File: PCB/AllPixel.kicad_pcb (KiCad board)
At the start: 2 copper layers, 68.5 x 24.5 mm, 28 parts, among them CON1 ML_USB_MINI, CON2 BARREL_JACK, Q1 NPN, U1 ATMEGA16U4/32U4, Y1 16MHz

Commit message: fixed silk screen on pads
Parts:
- U1: footprint TQFP44 -> TQFP44_FixedSilk

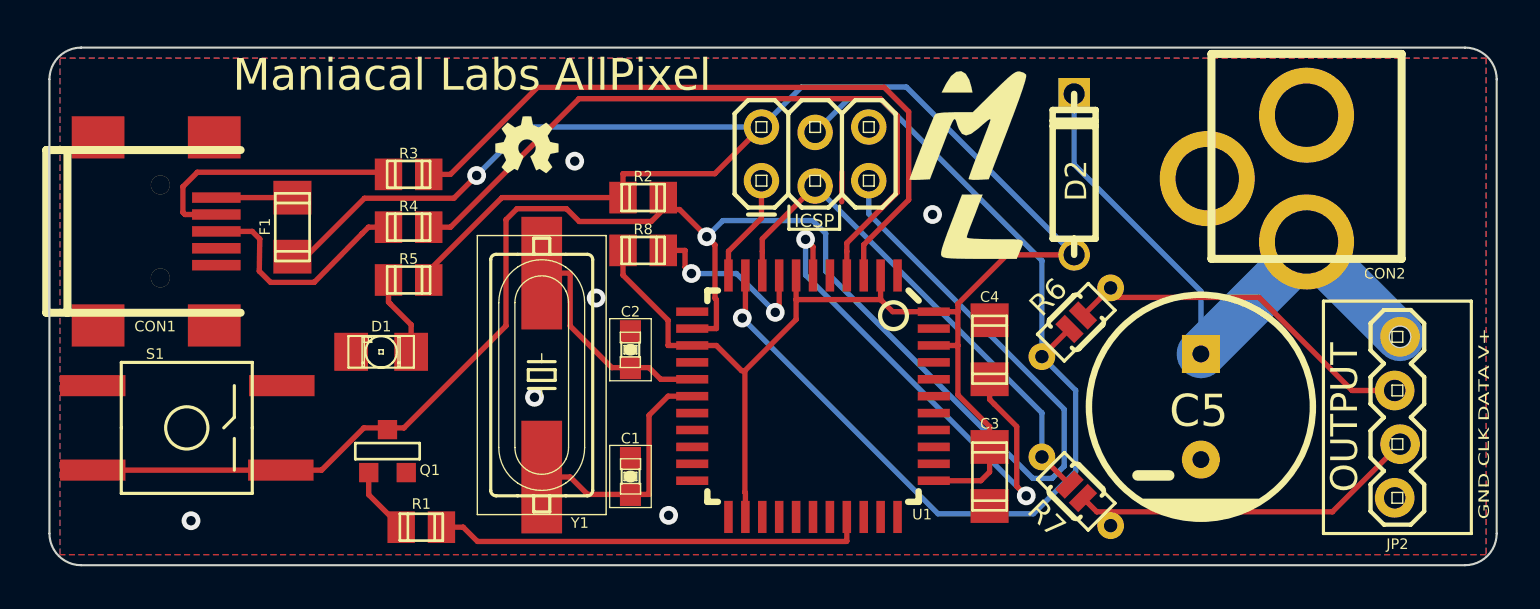
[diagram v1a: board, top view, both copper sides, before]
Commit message: further fixing of silk screen
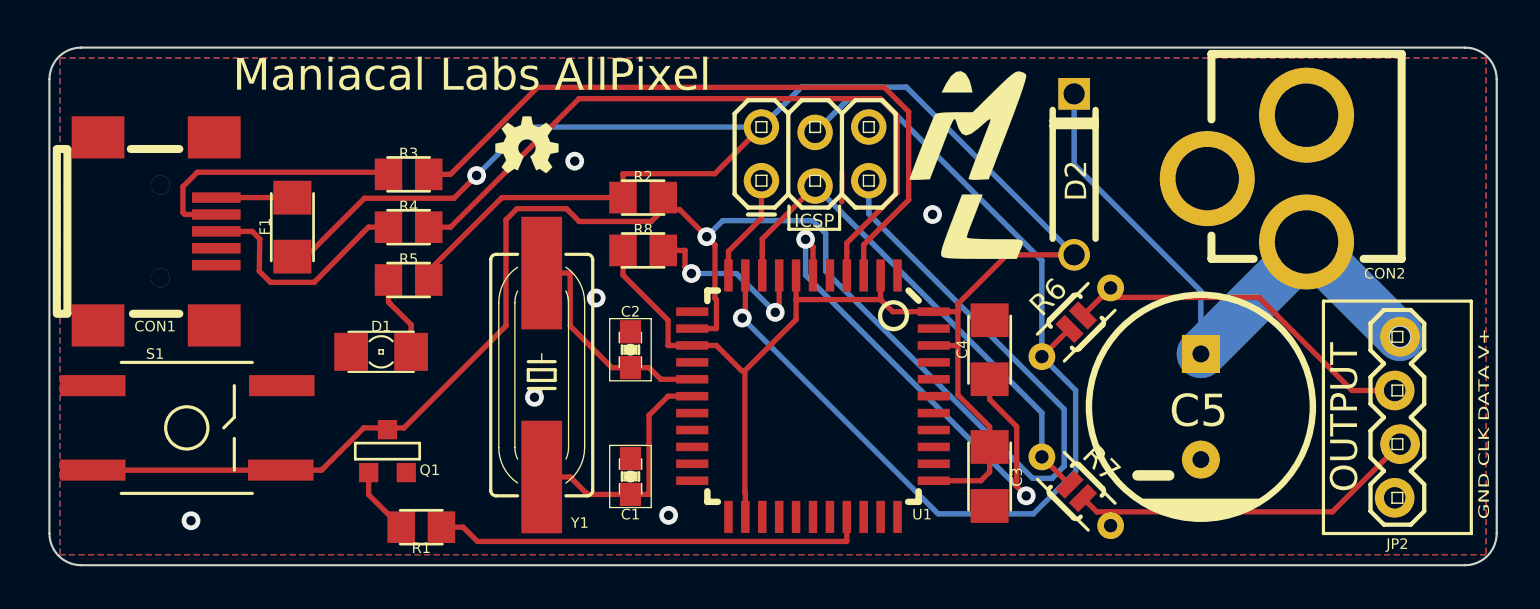
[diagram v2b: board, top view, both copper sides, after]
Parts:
- C3, C4, F1: footprint c_1206 -> ML_c_1206
- D1: footprint LED-1206 -> ML_LED-1206
- R1, R2, R3, R4, R5, R8: footprint c_0805 -> ML_c_0805
